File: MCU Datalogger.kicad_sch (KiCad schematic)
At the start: 25 parts, among them U1 24LC1025, U2 DS1337S+, U3 24LC1025, U4 ATMEGA328P-AU, Y1 32.768 KHz, Y2 16 MHz

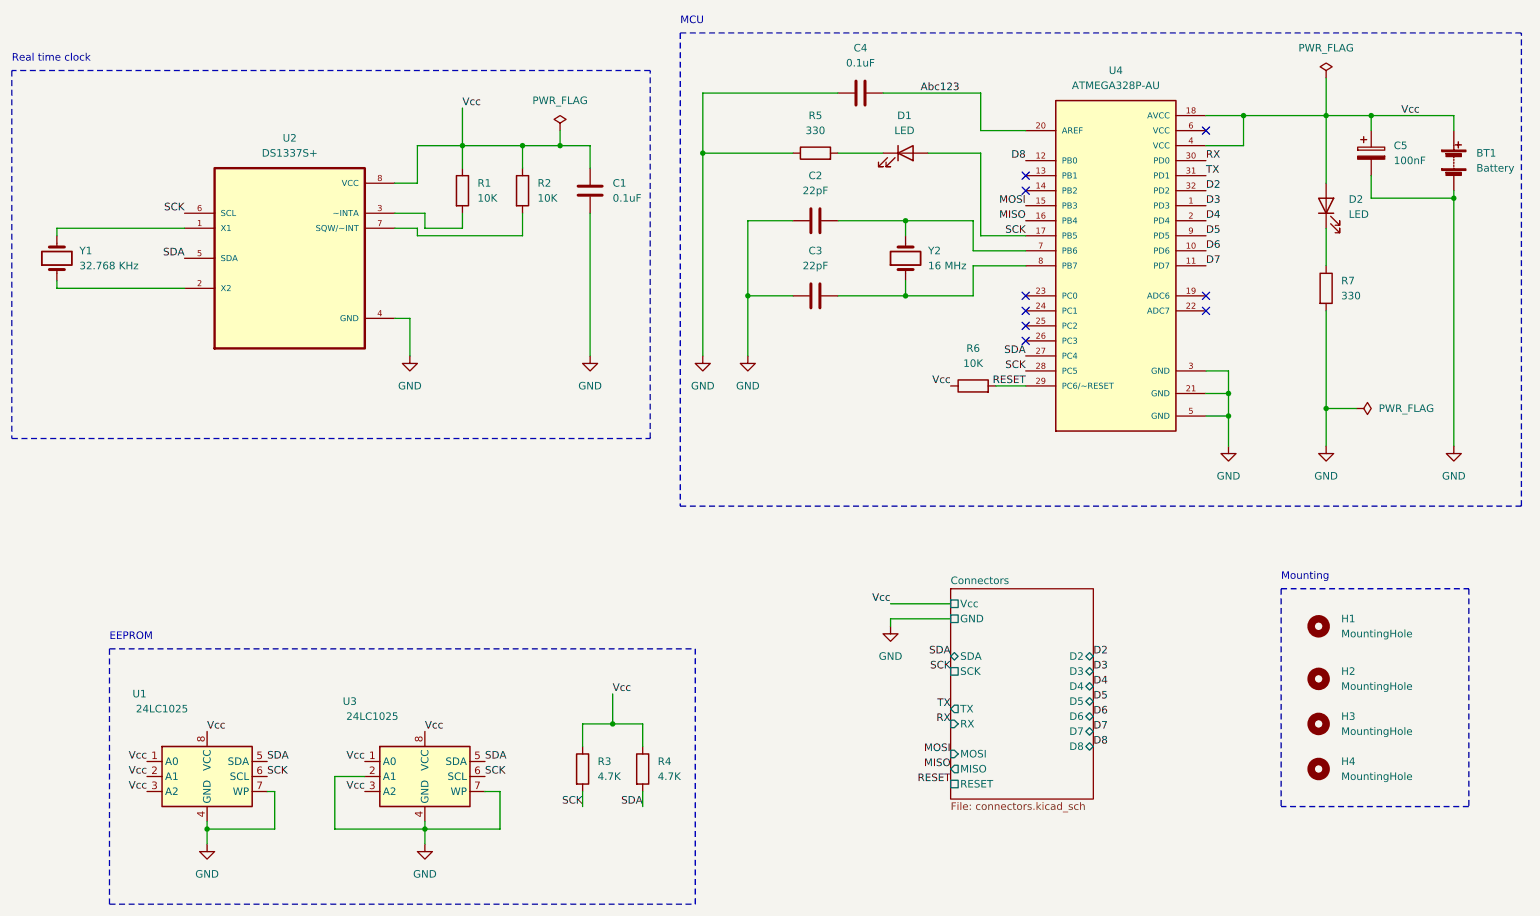
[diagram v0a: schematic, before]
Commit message: Fixed errata #106
I2C clock should be named SCL and not connected to SPI click net SCK
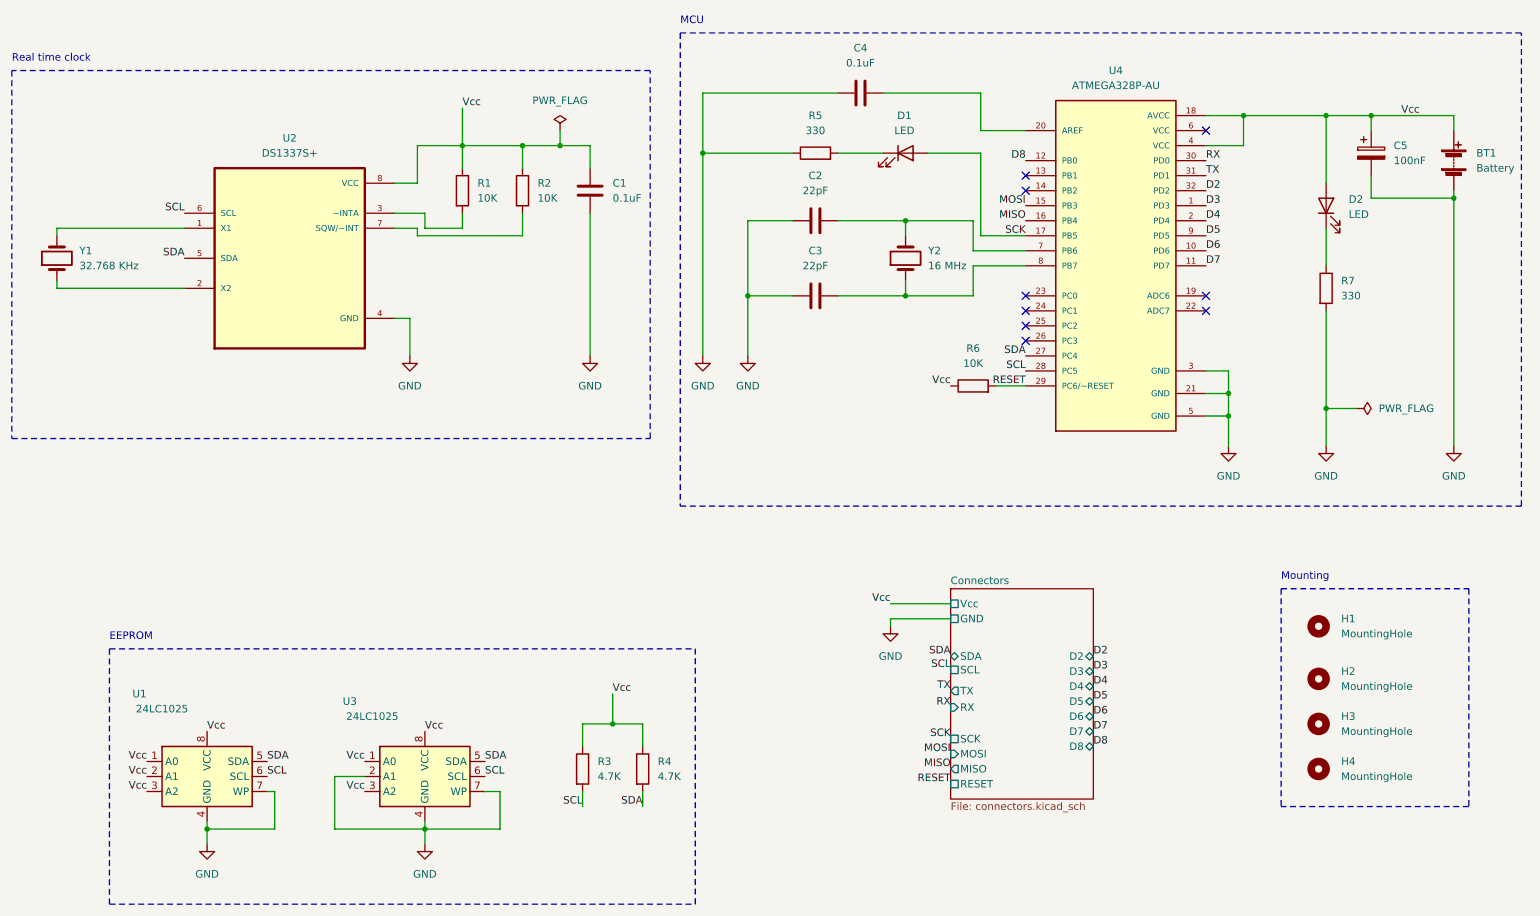
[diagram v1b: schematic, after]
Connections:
- net SCK: no longer R3.2, U1.6 (SCL), U2.6 (SCL), U3.6 (SCL), U4.28 (PC5)
- net Abc123: no longer names the net of C4.2, U4.20 (AREF)
- new net SCL: R3.2, U1.6 (SCL), U2.6 (SCL), U3.6 (SCL), U4.28 (PC5)
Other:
- sheet Connectors ports: added SCL; removed none
